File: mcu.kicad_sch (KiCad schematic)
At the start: 0 parts

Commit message: Chose amplifiers
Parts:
- added U9: NUCLEOH723ZG, NUCLEOH723ZG:MODULE_NUCLEOH723ZG, symbol NUCLEOH723ZG:NUCLEOH723ZG
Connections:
- new net: U9.CN10_10 (D3/TIMER_A_PWM3), U9.CN10_14 (D1/USART_A_TX), U9.CN10_16 (D0/USART_A_RX), U9.CN10_18 (D42/TIMER_A_PWM1N), U9.CN10_4 (D6/TIMER_A_PWM1), U9.CN10_7 (A6/ADC_A_IN), U9.CN10_9 (A7/ADC_B_IN), U9.CN8_11 (GND_CN8), U9.CN8_13 (GND_CN8), U9.CN8_14 (D49/IO), U9.CN8_16 (D50/IO)
- new net: U9.CN10_17 (GND_CN10), U9.CN10_22 (GND_CN10), U9.CN10_27 (GND_CN10), U9.CN10_5 (GND_CN10)
- new net: U9.CN3_1 (GND_CN3), U9.CN3_2 (GND_CN3)
- new net: U9.CN4_1 (GND_CN4), U9.CN4_2 (GND_CN4)
- new net: U9.CN15_1 (GND_CN15), U9.CN15_2 (GND_CN15)
- new net: U9.CN16_1 (GND_CN16), U9.CN16_2 (GND_CN16)
- new net: U9.CN12_20 (GND_CN12), U9.CN12_39 (GND_CN12), U9.CN12_54 (GND_CN12), U9.CN12_63 (GND_CN12), U9.CN12_9 (GND_CN12)
- new net: U9.CN11_10 (NC), U9.CN11_26 (NC), U9.CN11_67 (NC)
- new net: U9.CN11_19 (GND_CN11), U9.CN11_20 (GND_CN11), U9.CN11_22 (GND_CN11), U9.CN11_49 (GND_CN11), U9.CN11_60 (GND_CN11), U9.CN11_8 (GND_CN11)
- new net: U9.CN9_12 (GND_CN9), U9.CN9_23 (GND_CN9)

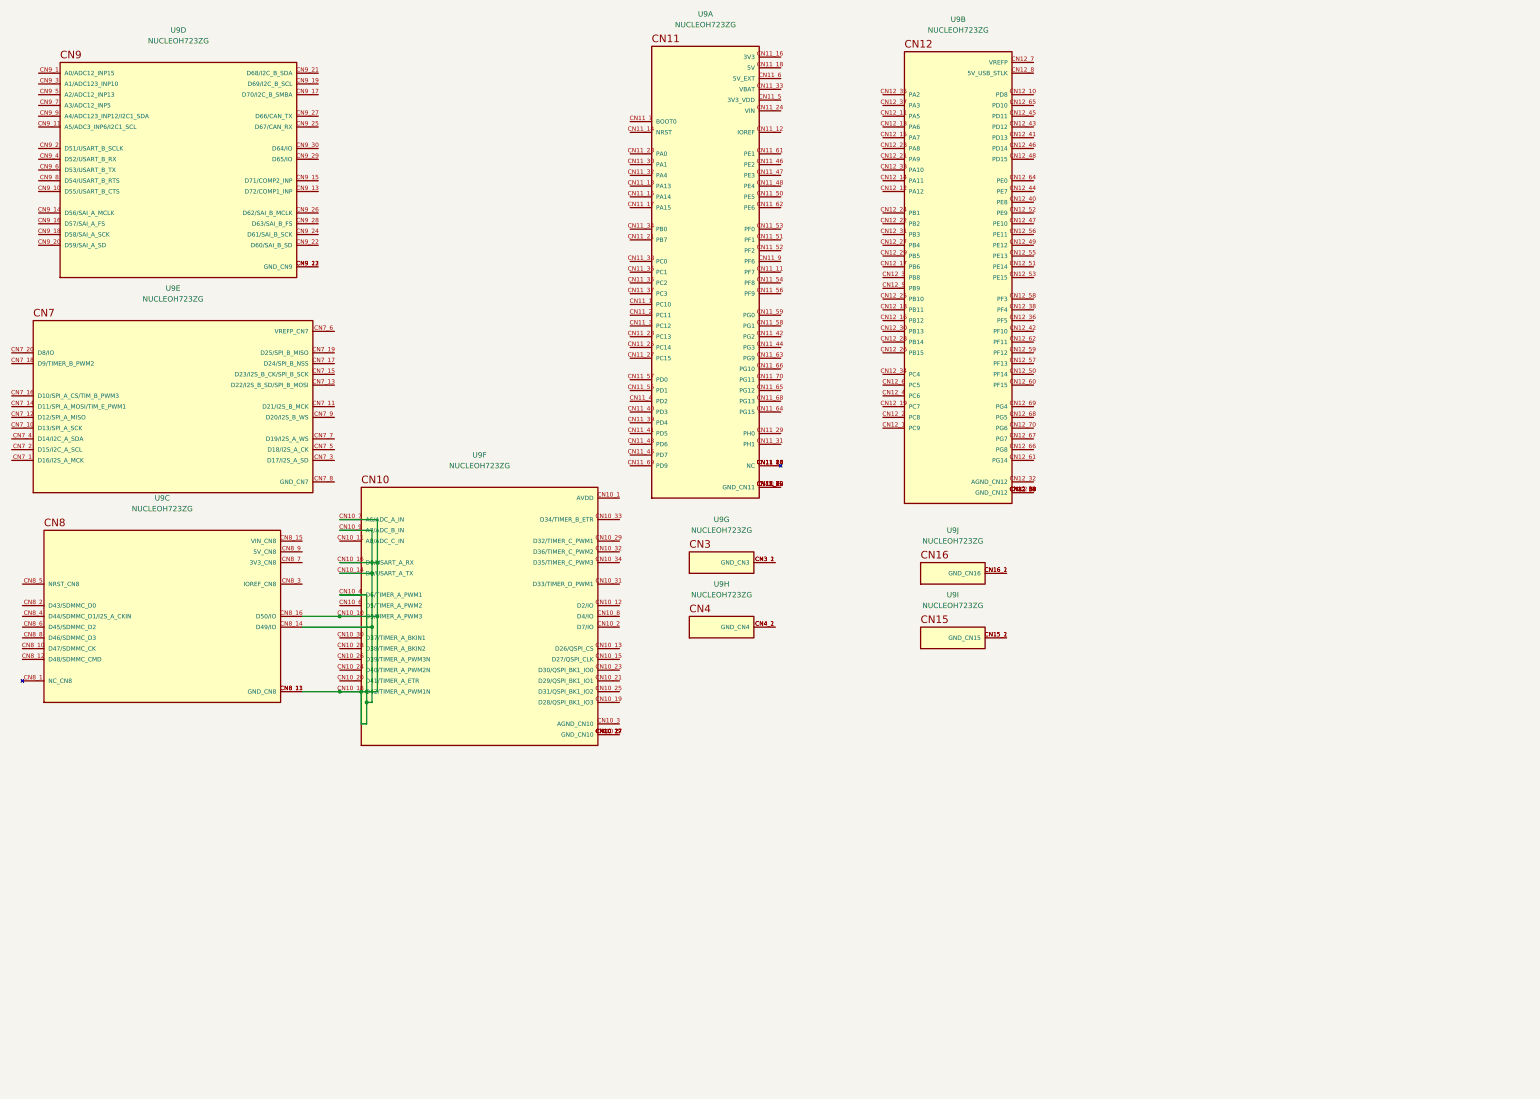
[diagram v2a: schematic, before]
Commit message: PCB edge, initial work on assigning footprints
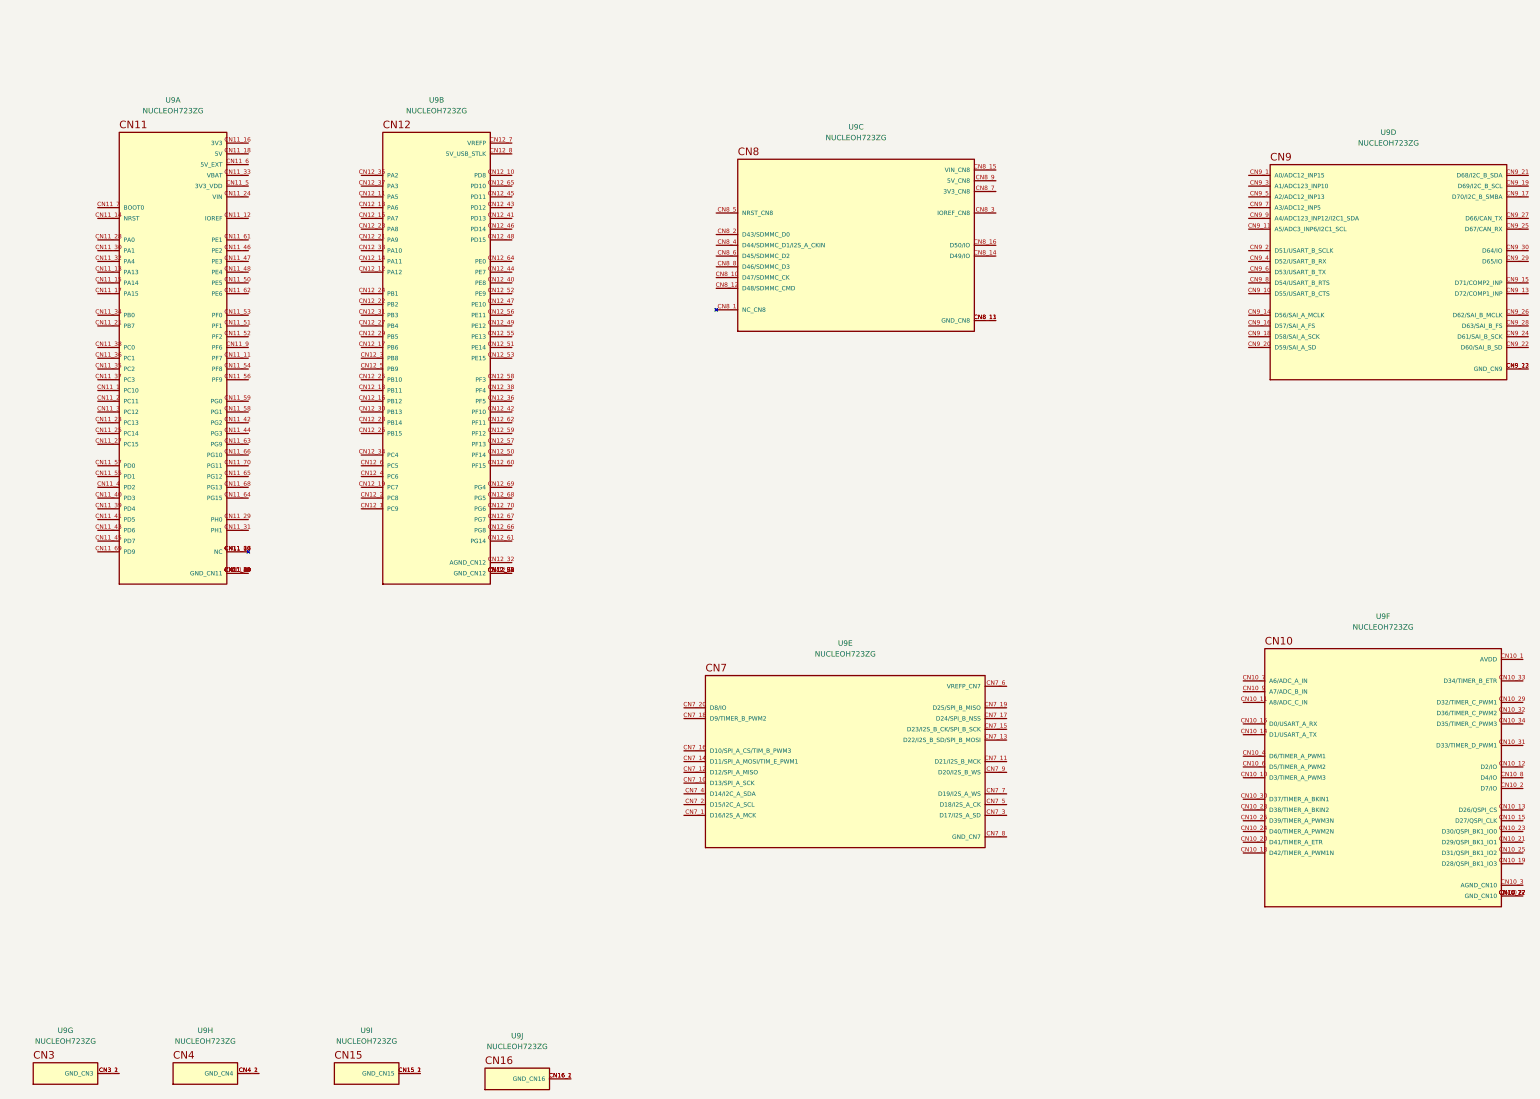
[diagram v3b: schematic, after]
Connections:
- new net: U9.CN8_11 (GND_CN8), U9.CN8_13 (GND_CN8)
- now unconnected: U9.CN10_10 (D3/TIMER_A_PWM3), U9.CN10_14 (D1/USART_A_TX), U9.CN10_16 (D0/USART_A_RX), U9.CN10_18 (D42/TIMER_A_PWM1N), U9.CN10_4 (D6/TIMER_A_PWM1), U9.CN10_7 (A6/ADC_A_IN), U9.CN10_9 (A7/ADC_B_IN), U9.CN8_14 (D49/IO), U9.CN8_16 (D50/IO)

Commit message: Link up ADC to FPGA
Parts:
- added TR1: Wuerth_749013011A, Transformer_SMD:Transformer_Ethernet_Wuerth_749013011A, symbol Transformer:Wuerth_749013011A
- added U28: STM32H723ZGIx, Package_BGA:UFBGA-144_7x7mm_Layout12x12_P0.5mm, symbol MCU_ST_STM32H7:STM32H723ZGIx
- added U29: LAN8742A, Package_DFN_QFN:VQFN-24-1EP_4x4mm_P0.5mm_EP2.5x2.5mm_ThermalVias, symbol Interface_Ethernet:LAN8742A
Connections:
- new net: U28.D2 (VSS), U28.E6 (VSS), U28.E7 (VSS), U28.G10 (VSS), U28.G4 (VSS), U28.G8 (VSS), U28.H5 (VSS), U28.H6 (VSS)
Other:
- moved on the sheet: U9A, U9B, U9C, U9D, U9E, U9F

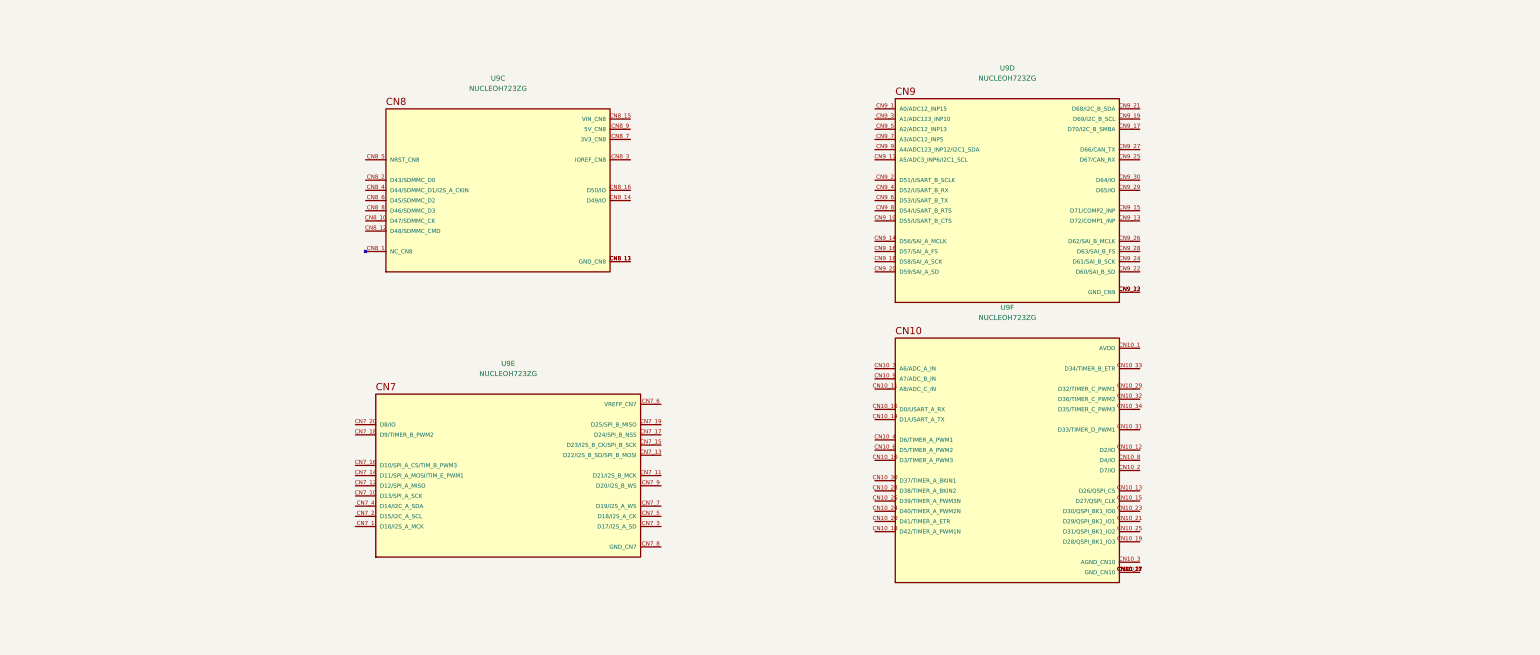
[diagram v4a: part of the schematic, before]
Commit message: Add connection between MCU and FPGA
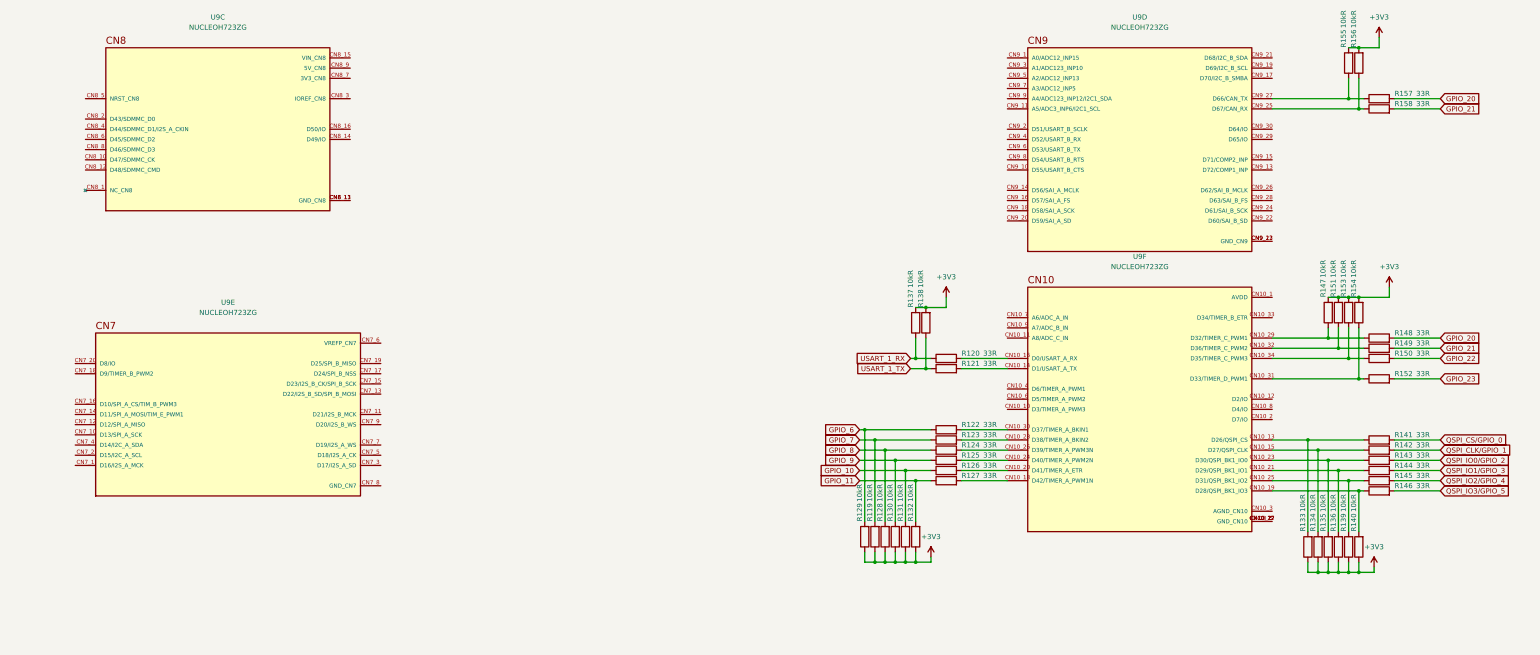
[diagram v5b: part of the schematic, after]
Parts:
- added R119, R128, R129, R130, R131, R132, R133, R134, R135, R136, R137, R138, R139, R140, R147, R151, R153, R154, R155, R156: 10kR, Resistor_SMD:R_0402_1005Metric_Pad0.72x0.64mm_HandSolder, symbol Device:R
- added R120, R121, R122, R123, R124, R125, R126, R127, R141, R142, R143, R144, R145, R146, R148, R149, R150, R152, R157, R158: 33R, Resistor_SMD:R_0402_1005Metric_Pad0.72x0.64mm_HandSolder, symbol Device:R
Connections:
- net at U9.CN9_25 (D67/CAN_RX): now also R156.1, R158.1
- net at U9.CN9_27 (D66/CAN_TX): now also R155.1, R157.1
- net at U9.CN10_13 (D26/QSPI_CS): now also R133.2, R141.1
- net at U9.CN10_14 (D1/USART_A_TX): now also R121.2
- net at U9.CN10_15 (D27/QSPI_CLK): now also R134.2, R142.1
- net at U9.CN10_16 (D0/USART_A_RX): now also R120.2
- net at U9.CN10_18 (D42/TIMER_A_PWM1N): now also R127.2
- net at U9.CN10_19 (D28/QSPI_BK1_IO3): now also R140.2, R146.1
- net at U9.CN10_20 (D41/TIMER_A_ETR): now also R126.2
- net at U9.CN10_21 (D29/QSPI_BK1_IO1): now also R136.2, R144.1
- net at U9.CN10_23 (D30/QSPI_BK1_IO0): now also R135.2, R143.1
- net at U9.CN10_24 (D40/TIMER_A_PWM2N): now also R125.2
- net at U9.CN10_25 (D31/QSPI_BK1_IO2): now also R139.2, R145.1
- net at U9.CN10_26 (D39/TIMER_A_PWM3N): now also R124.2
- net at U9.CN10_28 (D38/TIMER_A_BKIN2): now also R123.2
- net at U9.CN10_29 (D32/TIMER_C_PWM1): now also R147.1, R148.1
- net at U9.CN10_30 (D37/TIMER_A_BKIN1): now also R122.2
- net at U9.CN10_31 (D33/TIMER_D_PWM1): now also R152.1, R154.1
- net at U9.CN10_32 (D36/TIMER_C_PWM2): now also R149.1, R151.1
- net at U9.CN10_34 (D35/TIMER_C_PWM3): now also R150.1, R153.1
- new net +3V3: R119.1, R128.1, R129.1, R130.1, R131.1, R132.1, R133.1, R134.1, R135.1, R136.1, R137.2, R138.2, R139.1, R140.1, R147.2, R151.2, R153.2, R154.2, R155.2, R156.2
- new net GPIO_10: R126.1, R131.2
- new net GPIO_11: R127.1, R132.2
- new net GPIO_20: R148.2, R157.2
- new net GPIO_21: R149.2, R158.2
- new net GPIO_22: R150.2
- new net GPIO_23: R152.2
- new net GPIO_6: R122.1, R129.2
- new net GPIO_7: R119.2, R123.1
- new net GPIO_8: R124.1, R128.2
- new net GPIO_9: R125.1, R130.2
- new net QSPI_CLK/GPIO_1: R142.2
- new net QSPI_CS/GPIO_0: R141.2
- new net QSPI_IO0/GPIO_2: R143.2
- new net QSPI_IO1/GPIO_3: R144.2
- new net QSPI_IO2/GPIO_4: R145.2
- new net QSPI_IO3/GPIO_5: R146.2
- new net USART_1_RX: R120.1, R137.1
- new net USART_1_TX: R121.1, R138.1
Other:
- moved on the sheet: U9C, U9D, U9E, U9F

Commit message: Add things to MCU on the board
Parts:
- added C48, C49, C52, C53: C, symbol Device:C
- added C50, C51: 100nF, symbol Device:C
- added D11, D12: PTVS5V0Z1USK, Diode_SMD:Nexperia_DSN1608-2_1.6x0.8mm, symbol Diode:PTVS5V0Z1USK
- added J8: RJ45, symbol Connector:RJ45
- added R159, R169: 0R, symbol Device:R
- added R160, R161, R162, R167, R168, R170, R182: 0R, Resistor_SMD:R_0402_1005Metric_Pad0.72x0.64mm_HandSolder, symbol Device:R
- added R163, R164, R166, R171: 33R, Resistor_SMD:R_0402_1005Metric_Pad0.72x0.64mm_HandSolder, symbol Device:R
- added R165, R172, R173, R174, R175, R176: 10k, Resistor_SMD:R_0402_1005Metric_Pad0.72x0.64mm_HandSolder, symbol Device:R
- added R177, R178, R179, R180: 49.9R, Resistor_SMD:R_0402_1005Metric_Pad0.72x0.64mm_HandSolder, symbol Device:R
- added R181: 10K, symbol Device:R
- added R183, R184: 10K, Resistor_SMD:R_0402_1005Metric_Pad0.72x0.64mm_HandSolder, symbol Device:R
- added R185: 33R, symbol Device:R
- added R186: 100K, symbol Device:R
- added R189, R190, R191, R192: 10kR, Resistor_SMD:R_0402_1005Metric_Pad0.72x0.64mm_HandSolder, symbol Device:R
- added SW1, SW2: SW_DPST_x2, symbol Switch:SW_DPST_x2
- added Y1, Y2: Crystal_GND23, symbol Device:Crystal_GND23
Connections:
- net +3V3: now also R172.2, R173.2, R174.2, R175.2, R176.2, R177.2, R178.2, R179.2, R180.2, R189.1, R190.1, R191.1, R192.1
- net +3V3 MCU: now reaches U28.C11 (VDD33USB)
- net +3V3 MCU: now also U28.C2 (VBAT), U28.D3 (VDD), U28.F10 (VDD), U28.F4 (VDD), U28.F5 (VDD), U28.F6 (VDD), U28.F7 (VDD), U28.F8 (VDD), U28.F9 (VDD), U28.G5 (VDD), U28.G6 (VDD), U28.G7 (VDD), U9.CN8_15 (VIN_CN8), R159.2, R183.1, SW1.1 (A)
- net RMII_TX_EN: now reaches U28.C8 (PG11)
- net RMII_TX_EN: now also R162.1
- net PHO0: now reaches U28.D1 (PH0)
- net PHO0: now also C52.2, Y2.4
- net GND: now reaches U28.D2 (VSS), U28.E6 (VSS), U28.E7 (VSS), U28.G10 (VSS), U28.G4 (VSS), U28.G8 (VSS), U28.H5 (VSS), U28.H6 (VSS)
- net GND: now also U28.J1 (VSSA), U29.25 (VSS), U9.CN8_11 (GND_CN8), U9.CN8_13 (GND_CN8), U9.CN9_12 (GND_CN9), U9.CN9_23 (GND_CN9), C48.1, C49.1, C50.2, C51.2, C52.1, C53.1, D11.2 (A), D12.2 (A), R165.1, R181.1, R184.1, R186.1, SW2.2 (B), Y1.2, Y1.3, Y2.2, Y2.3
- net at U28.D5 (BOOT0): now also R181.2, R182.2
- net RMII_TXD0: now reaches U28.D7 (PG13)
- net RMII_TXD0: now also R161.1
- net PHO1: now reaches U28.E1 (PH1)
- net PHO1: now also C53.2, Y2.1
- net at U28.E5 (PDR_ON): now also R183.2, R184.2
- net NRST: now reaches U28.F1 (NRST)
- net NRST: now also U9.CN8_5 (NRST_CN8), C51.1, D12.1 (K), R170.1, SW2.1 (A)
- net RMII_MDC: now reaches U28.H2 (PC1)
- net RMII_MDC: now also R168.1
- net BUTTON_0: now reaches U28.J2 (PA0)
- net BUTTON_0: now also C50.1, R185.1
- net RMII_RXD0: now reaches U28.J4 (PC4)
- net RMII_RXD0: now also R163.1
- net RMII_REF_CLK: now reaches U28.K2 (PA1)
- net RMII_REF_CLK: now also R171.1
- net RMII_RXD1: now reaches U28.K4 (PC5)
- net RMII_RXD1: now also R164.1
- net RMII_MDIO: now reaches U28.L2 (PA2)
- net RMII_MDIO: now also R167.1
- net at U28.M1 (VDDA): now also R159.1
- net RMII_TXD1: now reaches U28.M12 (PB13)
- net RMII_TXD1: now also R160.1
- net RMII_CRS_DV: now reaches U28.M3 (PA7)
- net RMII_CRS_DV: now also R166.1
- net SPI_1_SCK: now reaches U9.CN7_10 (D13/SPI_A_SCK)
- net SPI_1_SCK: now also R192.2
- net SPI_1_MISO: now reaches U9.CN7_12 (D12/SPI_A_MISO)
- net SPI_1_MISO: now also R191.2
- net SPI_1_MOSI: now reaches U9.CN7_14 (D11/SPI_A_MOSI/TIM_E_PWM1)
- net SPI_1_MOSI: now also R190.2
- net SPI_1_CS: now reaches U9.CN7_16 (D10/SPI_A_CS/TIM_B_PWM3)
- net SPI_1_CS: now also R189.2
- net at U29.10 (RXER/PHYAD0): now also R165.2
- net at U29.11 (CRS_DV/MODE2): now also R166.2, R174.1
- net at U29.12 (MDIO): now also R167.2, R175.1
- net at U29.13 (MDC): now also R168.2
- net at U29.14 (~{INT}/REFCLKO): now also R171.2, R176.1
- net at U29.15 (~{RST}): now also R170.2
- net at U29.16 (TXEN): now also R162.2
- net at U29.17 (TXD0): now also R161.2
- net at U29.18 (TXD1): now also R160.2
- net at U29.20 (TXN): now also TR1.6 (RD+), R178.1
- net at U29.21 (TXP): now also TR1.8 (RD-), R177.1
- net at U29.22 (RXN): now also TR1.1 (TD+), R180.1
- net at U29.23 (RXP): now also TR1.3 (TD-), R179.1
- net at U29.4 (XTAL2): now also R169.1
- net at U29.5 (XTAL1/CLKIN): now also C48.2, Y1.4
- net at U29.7 (RXD1/MODE1): now also R164.2, R173.1
- net at U29.8 (RXD0/MODE0): now also R163.2, R172.1
- net at TR1.11 (RX+): now also J8.2
- net at TR1.14 (TX-): now also J8.3
- net at TR1.16 (TX+): now also J8.4
- net at TR1.9 (RX-): now also J8.1
- new net: D11.1 (K), R185.2, R186.2, SW1.2 (B)
- new net: C49.2, R169.2, Y1.1
- new net BOOT0: R182.1
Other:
- note added: "TODO: 25 MHz"
- note added: "TODO: Change connector"
- note added: "Unused"
- moved on the sheet: R119, R120, R121, R122, R123, R124, R125, R126, R127, R128, R129, R130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
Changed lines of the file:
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@@
 	(generator "eeschema")
 	(generator_version "9.0")
-	(paper "A3")
+	(paper "A2")

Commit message: Save work on simplifying the desing
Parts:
- removed C48, C49, C52, C53: C, symbol Device:C
- removed C50, C51: 100nF, symbol Device:C
- removed D11, D12: PTVS5V0Z1USK, Diode_SMD:Nexperia_DSN1608-2_1.6x0.8mm, symbol Diode:PTVS5V0Z1USK
- removed J8: RJ45, symbol Connector:RJ45
- removed R159, R169: 0R, symbol Device:R
- removed R160, R161, R162, R167, R168, R170, R182: 0R, Resistor_SMD:R_0402_1005Metric_Pad0.72x0.64mm_HandSolder, symbol Device:R
- removed R163, R164, R166, R171: 33R, Resistor_SMD:R_0402_1005Metric_Pad0.72x0.64mm_HandSolder, symbol Device:R
- removed R165, R172, R173, R174, R175, R176: 10k, Resistor_SMD:R_0402_1005Metric_Pad0.72x0.64mm_HandSolder, symbol Device:R
- removed R177, R178, R179, R180: 49.9R, Resistor_SMD:R_0402_1005Metric_Pad0.72x0.64mm_HandSolder, symbol Device:R
- removed R181: 10K, symbol Device:R
- removed R183, R184: 10K, Resistor_SMD:R_0402_1005Metric_Pad0.72x0.64mm_HandSolder, symbol Device:R
- removed R185: 33R, symbol Device:R
- removed R186: 100K, symbol Device:R
- removed SW1, SW2: SW_DPST_x2, symbol Switch:SW_DPST_x2
- removed TR1: Wuerth_749013011A, Transformer_SMD:Transformer_Ethernet_Wuerth_749013011A, symbol Transformer:Wuerth_749013011A
- removed U28: STM32H723ZGIx, Package_BGA:UFBGA-144_7x7mm_Layout12x12_P0.5mm, symbol MCU_ST_STM32H7:STM32H723ZGIx
- removed U29: LAN8742A, Package_DFN_QFN:VQFN-24-1EP_4x4mm_P0.5mm_EP2.5x2.5mm_ThermalVias, symbol Interface_Ethernet:LAN8742A
- removed Y1, Y2: Crystal_GND23, symbol Device:Crystal_GND23
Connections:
- net +5V: now reaches U9.CN8_9 (5V_CN8)
- net +3V3 MCU: no longer names the net of U9.CN8_15 (VIN_CN8)
- no-connect marks 0 -> 2
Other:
- note removed: "TODO: 25 MHz"
- note removed: "TODO: Change connector"
- moved on the sheet: R119, R120, R121, R122, R123, R124, R125, R126, R127, R128, R129, R130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
